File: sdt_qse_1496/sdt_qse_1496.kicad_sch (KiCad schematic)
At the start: 59 parts, among them J1 Conn_02x08_Odd_Even, J2 SJ-3524-SMT, J3 5-1814832-1, J4 5-1814832-1, J6 Conn_01x02_Male, Q1 Q_NPN_BEC, Q2 Q_NPN_BEC, Q3 Q_PMOS_GSD, Q4 Q_PMOS_GSD, Q5 Q_NPN_BEC, Q6 Q_NPN_BEC, U1 SN74AC74PW, U3 0553-0013-BC-F

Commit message: Released version 2.0 PCB.
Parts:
- R13, R14: value 500 -> 470
- R65, R68: value 100 -> DNP
- R66: value 100 -> 0
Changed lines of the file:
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@@
       (effects (font (size 1.27 1.27)) (justify right))
     )
-    (property "Value" "100" (id 1) (at 245.491 72.8222 0)
+    (property "Value" "DNP" (id 1) (at 245.491 72.8222 0)
       (effects (font (size 1.27 1.27)) (justify right))
     )
@@
     (in_bom yes) (on_board yes) (fields_autoplaced)
     (property "Reference" "R13" (id 0) (at 138.43 38.5912 90))
-    (property "Value" "500" (id 1) (at 138.43 41.1281 90))
+    (property "Value" "470" (id 1) (at 138.43 41.1281 90))
     (property "Footprint" "Resistor_SMD:R_1206_3216Metric" (id 2) (at 138.176 44.196 90)
       (effects (font (size 1.27 1.27)) hide)
@@
       (effects (font (size 1.27 1.27)) (justify right))
     )
-    (property "Value" "100" (id 1) (at 234.061 72.8222 0)
+    (property "Value" "DNP" (id 1) (at 234.061 72.8222 0)
       (effects (font (size 1.27 1.27)) (justify right))
     )
@@
     (in_bom yes) (on_board yes) (fields_autoplaced)
     (property "Reference" "R14" (id 0) (at 138.43 86.8512 90))
-    (property "Value" "500" (id 1) (at 138.43 89.3881 90))
+    (property "Value" "470" (id 1) (at 138.43 89.3881 90))
     (property "Footprint" "Resistor_SMD:R_1206_3216Metric" (id 2) (at 138.176 92.456 90)
       (effects (font (size 1.27 1.27)) hide)
@@
     (in_bom yes) (on_board yes) (fields_autoplaced)
     (property "Reference" "R66" (id 0) (at 238.76 61.4512 90))
-    (property "Value" "100" (id 1) (at 238.76 63.9881 90))
+    (property "Value" "0" (id 1) (at 238.76 63.9881 90))
     (property "Footprint" "Resistor_SMD:R_1206_3216Metric" (id 2) (at 239.014 65.024 90)
       (effects (font (size 1.27 1.27)) hide)
@@
     )
     (path "/6a318012-90af-4c46-97b4-20766224a6af"
-      (reference "R13") (unit 1) (value "500") (footprint "Resistor_SMD:R_1206_3216Metric")
+      (reference "R13") (unit 1) (value "470") (footprint "Resistor_SMD:R_1206_3216Metric")
     )
     (path "/8c2b7f7b-f612-416e-9598-a027f07b1876"
-      (reference "R14") (unit 1) (value "500") (footprint "Resistor_SMD:R_1206_3216Metric")
+      (reference "R14") (unit 1) (value "470") (footprint "Resistor_SMD:R_1206_3216Metric")
     )
     (path "/2e64607a-d8d4-4a13-9ace-2b889e2da0e1"
@@
     )
     (path "/6fdbcc23-d1b7-4ef9-a817-5fc13bf8335e"
-      (reference "R65") (unit 1) (value "100") (footprint "Resistor_SMD:R_1206_3216Metric")
+      (reference "R65") (unit 1) (value "DNP") (footprint "Resistor_SMD:R_1206_3216Metric")
     )
     (path "/8ec21b16-2b3b-4d2e-8bbd-c59cff03e60c"
-      (reference "R66") (unit 1) (value "100") (footprint "Resistor_SMD:R_1206_3216Metric")
+      (reference "R66") (unit 1) (value "0") (footprint "Resistor_SMD:R_1206_3216Metric")
     )
     (path "/c463e771-2e52-4f16-9eb0-c0d321a9c87f"
@@
     )
     (path "/3bf728cf-20ea-46fe-b64d-226e7a8fbee5"
-      (reference "R68") (unit 1) (value "100") (footprint "Resistor_SMD:R_1206_3216Metric")
+      (reference "R68") (unit 1) (value "DNP") (footprint "Resistor_SMD:R_1206_3216Metric")
     )
     (path "/ff6a95e7-6bc1-4212-9c76-7fe6401cd2b8/dfa97546-f6d3-4d29-b3f5-f358956d3eda"

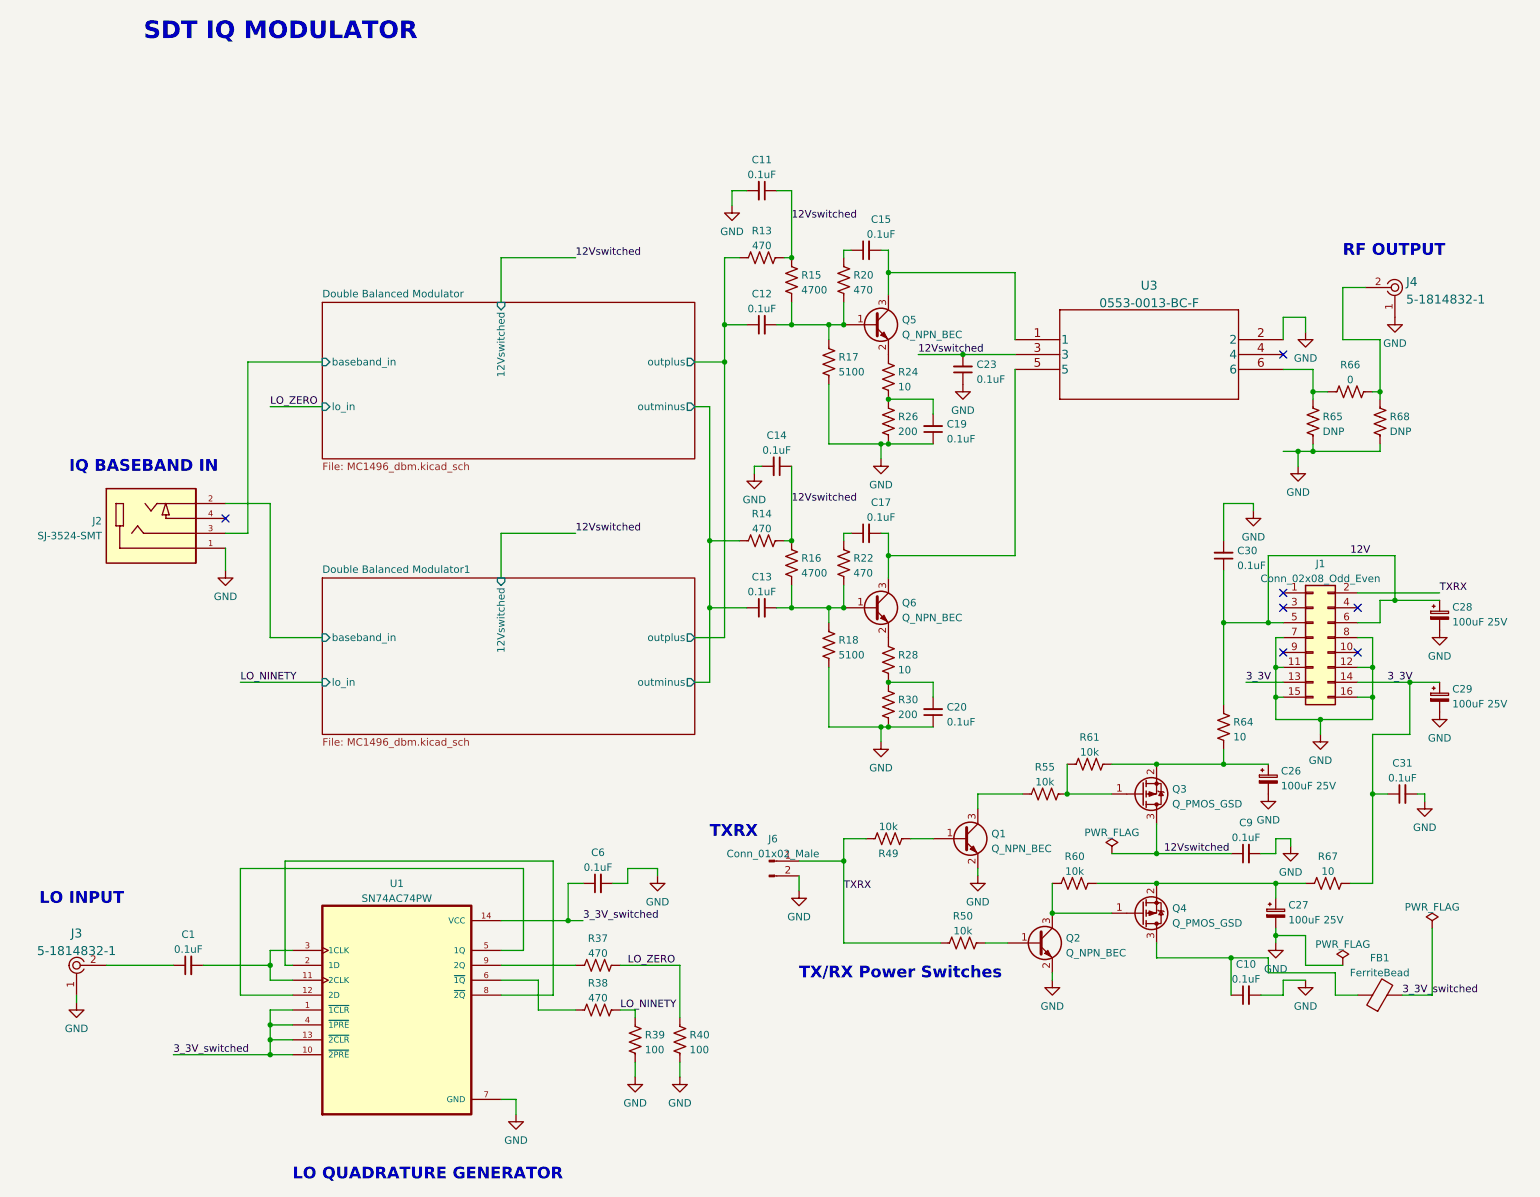
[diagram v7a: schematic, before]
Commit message: Added Sallen Key filters to schematic.
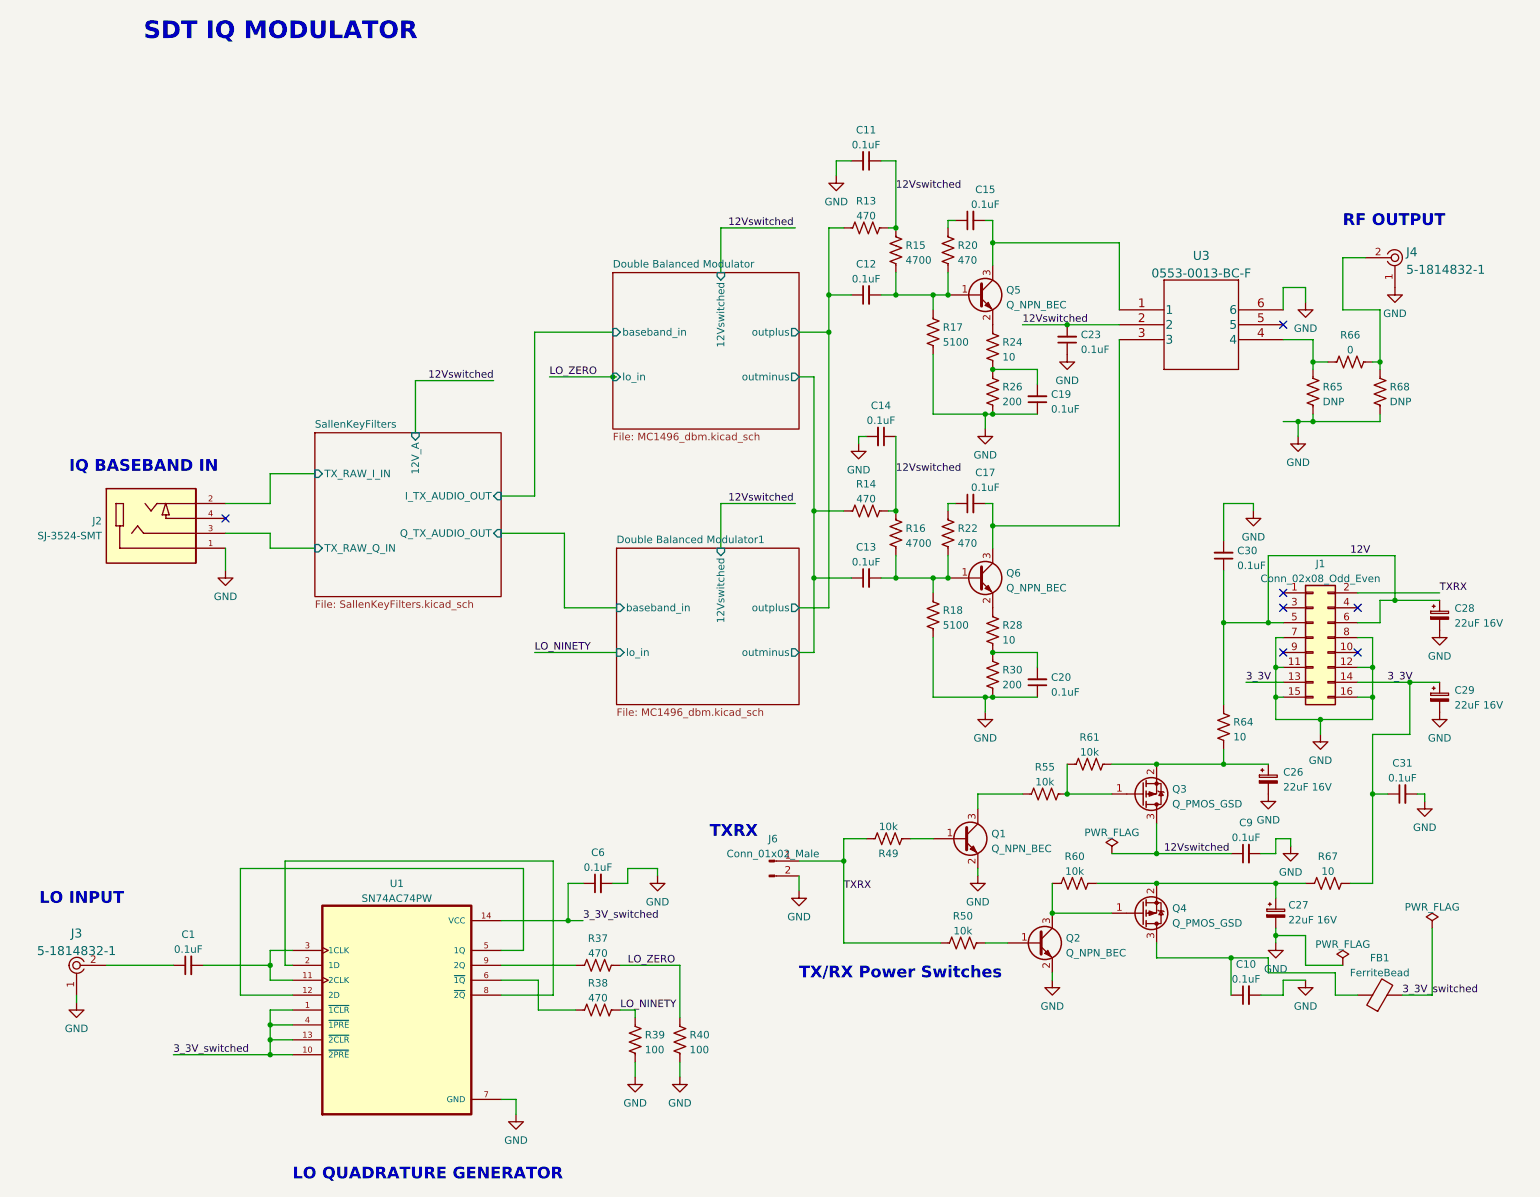
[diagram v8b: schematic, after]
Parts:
- C26, C27, C28, C29: value 100uF 25V -> 22uF 16V; footprint Capacitor_THT:CP_Radial_D8.0mm_P3.50mm -> Capacitor_SMD:C_1206_3216Metric
- U3: footprint Pulse_Transformer:0553-0013-BC-F -> 0553-0013_BEL:0553-0013-BC-F
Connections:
- net 12Vswitched: now also U3.2; no longer U3.3
- net Double Balanced Modulator/baseband_in: no longer J2.3
- net Double Balanced Modulator1/baseband_in: no longer J2.2
- net GND: now also U3.6; no longer U3.2
- net at C17.2, Q6.3 (C): now also U3.3; no longer U3.5
- net at R65.2, R66.1: now also U3.4; no longer U3.6
- new net SallenKeyFilters/TX_RAW_I_IN: J2.2
- new net SallenKeyFilters/TX_RAW_Q_IN: J2.3
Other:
- added sheet SallenKeyFilters (SallenKeyFilters.kicad_sch)
- moved on the sheet: C11, C12, C13, C14, C15, C17, C19, C20, C23, J4, Q5, Q6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
